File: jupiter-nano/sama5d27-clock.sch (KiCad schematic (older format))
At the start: 1 part

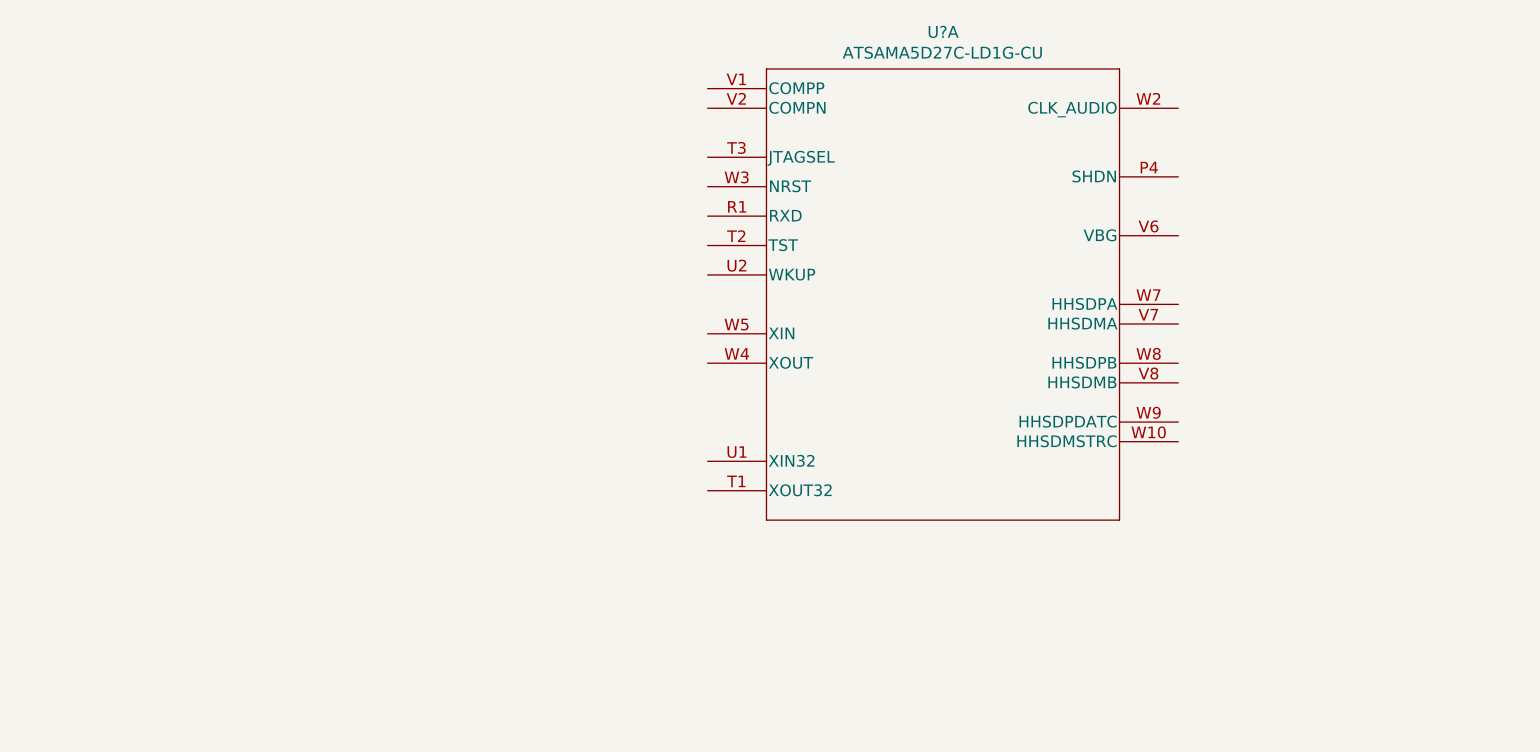
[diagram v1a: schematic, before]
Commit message: WIP some work on clocking
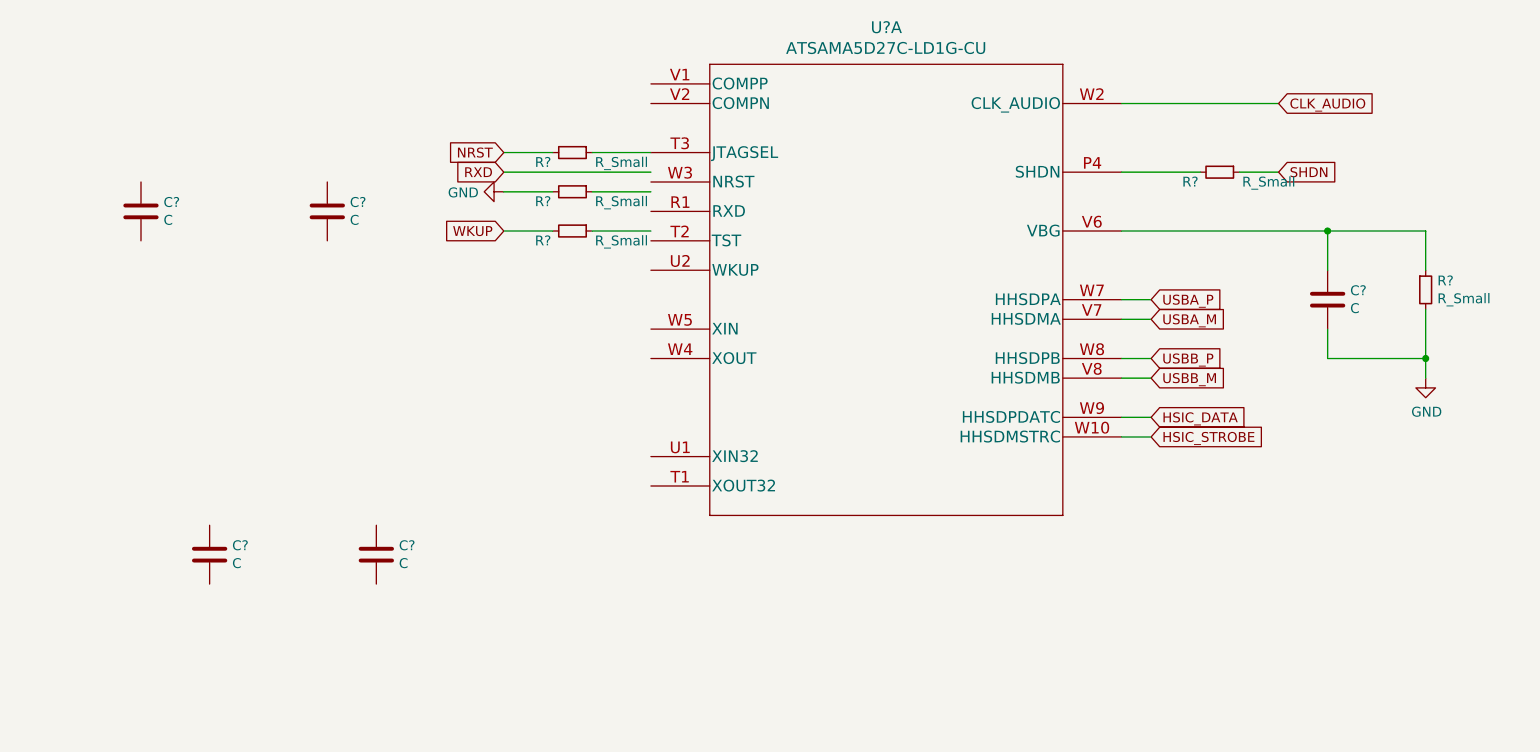
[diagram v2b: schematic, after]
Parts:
- added C? (x5): C, symbol Device:C
- added R? (x5): R_Small, symbol Device:R_Small
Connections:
- net labels added: CLK_AUDIO, GND, HSIC_DATA, HSIC_STROBE, NRST, RXD, SHDN, USBA_M, USBA_P, USBB_M, USBB_P, WKUP
- wire segments 0 -> 24
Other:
- moved on the sheet: U?A
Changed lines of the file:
@@
 L ATSAMA5D27C-LD1G:ATSAMA5D27C-LD1G-CU U?
 U 1 1 5F5D995F
-P 4739 2474
-F 0 "U?" H 5939 2961 60  0000 C CNN
-F 1 "ATSAMA5D27C-LD1G-CU" H 5939 2855 60  0000 C CNN
-F 2 "TFBGA361_16X16_MCH" H 5939 2814 60  0001 C CNN
-F 3 "" H 4739 2474 60  0000 C CNN
-	1    4739 2474
-	1    0    0    -1
-$EndComp
+P 4450 2450
+F 0 "U?" H 5650 2937 60  0000 C CNN
+F 1 "ATSAMA5D27C-LD1G-CU" H 5650 2831 60  0000 C CNN
+F 2 "TFBGA361_16X16_MCH" H 5650 2790 60  0001 C CNN
+F 3 "" H 4450 2450 60  0000 C CNN
+	1    4450 2450
+	1    0    0    -1
+$EndComp
+$Comp
+L Device:C C?
+U 1 1 5FB8C3A7
+P 1850 2900
+F 0 "C?" H 1965 2946 50  0000 L CNN
+F 1 "C" H 1965 2855 50  0000 L CNN
+F 2 "" H 1888 2750 50  0001 C CNN
+F 3 "~" H 1850 2900 50  0001 C CNN
+	1    1850 2900
+	1    0    0    -1
+$EndComp
+$Comp
+L Device:C C?
+U 1 1 5FB8D41E
+P 2800 2900
+F 0 "C?" H 2915 2946 50  0000 L CNN
+F 1 "C" H 2915 2855 50  0000 L CNN
+F 2 "" H 2838 2750 50  0001 C CNN
+F 3 "~" H 2800 2900 50  0001 C CNN
+	1    2800 2900
+	1    0    0    -1
+$EndComp
+$Comp
+L Device:C C?
+U 1 1 5FB8DCD9
+P 2200 4650
+F 0 "C?" H 2315 4696 50  0000 L CNN
+F 1 "C" H 2315 4605 50  0000 L CNN
+F 2 "" H 2238 4500 50  0001 C CNN
+F 3 "~" H 2200 4650 50  0001 C CNN
+	1    2200 4650
+	1    0    0    -1
+$EndComp
+$Comp
+L Device:C C?
+U 1 1 5FB8E15B
+P 3050 4650
+F 0 "C?" H 3165 4696 50  0000 L CNN
+F 1 "C" H 3165 4605 50  0000 L CNN
+F 2 "" H 3088 4500 50  0001 C CNN
+F 3 "~" H 3050 4650 50  0001 C CNN
+	1    3050 4650
+	1    0    0    -1
+$EndComp
+$Comp
+L Device:C C?
+U 1 1 5FB8E9C8
+P 7900 3350
+F 0 "C?" H 8015 3396 50  0000 L CNN
+F 1 "C" H 8015 3305 50  0000 L CNN
+F 2 "" H 7938 3200 50  0001 C CNN
+F 3 "~" H 7900 3350 50  0001 C CNN
+	1    7900 3350
+	1    0    0    -1
+$EndComp
+$Comp
+L Device:R_Small R?
+U 1 1 5FB8F66D
+P 8400 3300
+F 0 "R?" H 8459 3346 50  0000 L CNN
+F 1 "R_Small" H 8459 3255 50  0000 L CNN
+F 2 "" H 8400 3300 50  0001 C CNN
+F 3 "~" H 8400 3300 50  0001 C CNN
+	1    8400 3300
+	1    0    0    -1
+$EndComp
+$Comp
+L Device:R_Small R?
+U 1 1 5FB9019B
+P 4050 2600
+F 0 "R?" V 4100 2450 50  0000 C CNN
+F 1 "R_Small" V 4100 2850 50  0000 C CNN
+F 2 "" H 4050 2600 50  0001 C CNN
+F 3 "~" H 4050 2600 50  0001 C CNN
+	1    4050 2600
+	0    1    1    0
+$EndComp
+$Comp
+L Device:R_Small R?
+U 1 1 5FB90BC4
+P 4050 3000
+F 0 "R?" V 4100 2850 50  0000 C CNN
+F 1 "R_Small" V 4100 3250 50  0000 C CNN
+F 2 "" H 4050 3000 50  0001 C CNN
+F 3 "~" H 4050 3000 50  0001 C CNN
+	1    4050 3000
+	0    1    1    0
+$EndComp
+$Comp
+L Device:R_Small R?
+U 1 1 5FB913F4
+P 7350 2700
+F 0 "R?" V 7400 2550 50  0000 C CNN
+F 1 "R_Small" V 7400 2950 50  0000 C CNN
+F 2 "" H 7350 2700 50  0001 C CNN
+F 3 "~" H 7350 2700 50  0001 C CNN
+	1    7350 2700
+	0    1    1    0
+$EndComp
+$Comp
+L Device:R_Small R?
+U 1 1 5FB91AFA
+P 4050 2800
+F 0 "R?" V 4100 2650 50  0000 C CNN
+F 1 "R_Small" V 4100 3050 50  0000 C CNN
+F 2 "" H 4050 2800 50  0001 C CNN
+F 3 "~" H 4050 2800 50  0001 C CNN
+	1    4050 2800
+	0    1    1    0
+$EndComp
+Wire Wire Line
+	4450 2600 4150 2600
+Wire Wire Line
+	3950 2600 3700 2600
+Text GLabel 3700 2600 0    50   Input ~ 0
+NRST
+Text GLabel 3700 3000 0    50   Input ~ 0
+WKUP
+Wire Wire Line
+	4150 3000 4450 3000
+Wire Wire Line
+	3950 3000 3700 3000
+Wire Wire Line
+	6850 2700 7250 2700
+Wire Wire Line
+	7450 2700 7650 2700
+Text GLabel 7650 2700 2    50   Input ~ 0
+SHDN
+Wire Wire Line
+	4150 2800 4450 2800
+Wire Wire Line
+	3700 2800 3950 2800
+$Comp
+L power:GND #PWR?
+U 1 1 5FBB7C84
+P 3700 2800
+F 0 "#PWR?" H 3700 2550 50  0001 C CNN
+F 1 "GND" V 3705 2672 50  0000 R CNN
+F 2 "" H 3700 2800 50  0001 C CNN
+F 3 "" H 3700 2800 50  0001 C CNN
+	1    3700 2800
+	0    1    1    0
+$EndComp
+Wire Wire Line
+	4450 2700 3700 2700
+Text GLabel 3700 2700 0    50   Input ~ 0
+RXD
+Wire Wire Line
+	6850 2350 7650 2350
+Text GLabel 7650 2350 2    50   Input ~ 0
+CLK_AUDIO
+Wire Wire Line
+	6850 3000 7900 3000
+Wire Wire Line
+	7900 3000 7900 3200
+Wire Wire Line
+	7900 3000 8400 3000
+Wire Wire Line
+	8400 3000 8400 3200
+Connection ~ 7900 3000
+Wire Wire Line
+	8400 3400 8400 3650
+Wire Wire Line
+	8400 3650 7900 3650
+Wire Wire Line
+	7900 3650 7900 3500
+Wire Wire Line
+	8400 3650 8400 3750
+Connection ~ 8400 3650
+$Comp
+L power:GND #PWR?
+U 1 1 5FBD26A3
+P 8400 3750
+F 0 "#PWR?" H 8400 3500 50  0001 C CNN
+F 1 "GND" H 8405 3577 50  0000 C CNN
+F 2 "" H 8400 3750 50  0001 C CNN
+F 3 "" H 8400 3750 50  0001 C CNN
+	1    8400 3750
+	1    0    0    -1
+$EndComp
+Wire Wire Line
+	6850 3950 7000 3950
+Wire Wire Line
+	6850 4050 7000 4050
+Wire Wire Line
+	6850 3750 7000 3750
+Wire Wire Line
+	6850 3650 7000 3650
+Wire Wire Line
+	6850 3450 7000 3450
+Wire Wire Line
+	6850 3350 7000 3350
+Text GLabel 7000 3350 2    50   Input ~ 0
+USBA_P
+Text GLabel 7000 3450 2    50   Input ~ 0
+USBA_M
+Text GLabel 7000 3650 2    50   Input ~ 0
+USBB_P
+Text GLabel 7000 3750 2    50   Input ~ 0
+USBB_M
+Text GLabel 7000 3950 2    50   Input ~ 0
+HSIC_DATA
+Text GLabel 7000 4050 2    50   Input ~ 0
+HSIC_STROBE
 $EndSCHEMATC

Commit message: WIP clocking done
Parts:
- removed C?: C, symbol Device:C
- added C97: 8pF 50V, symbol Device:C
- added Y1: NX2012SA-32.768KHZ-EXS00A-MU00389, symbol Device:Crystal
- added Y2: NX3225SA-12MHZ-STD-CSR-3, symbol Device:Crystal_GND24
- C96: renamed from C?; value C -> 8pF 50V
- C98, C99: renamed from C?; value C -> 27pF 50V
- gave numbers to parts that had none: 1
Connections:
- wire segments 24 -> 47
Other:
- moved on the sheet: C96, C98, C99, R?

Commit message: WIP, PIO done
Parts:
- C98, C99: value 27pF 50V -> 16pF 50V
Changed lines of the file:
@@
 P 1300 3900
 F 0 "C98" H 1415 3946 50  0000 L CNN
-F 1 "27pF 50V" H 1415 3855 50  0000 L CNN
+F 1 "16pF 50V" H 1415 3855 50  0000 L CNN
 F 2 "" H 1338 3750 50  0001 C CNN
 F 3 "~" H 1300 3900 50  0001 C CNN
@@
 P 2250 3900
 F 0 "C99" H 2365 3946 50  0000 L CNN
-F 1 "27pF 50V" H 2365 3855 50  0000 L CNN
+F 1 "16pF 50V" H 2365 3855 50  0000 L CNN
 F 2 "" H 2288 3750 50  0001 C CNN
 F 3 "~" H 2250 3900 50  0001 C CNN

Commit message: WIP, connectors almost done
- still to do:
  - JTAG signals on PIO pins
  - USB-UART bridge
  - extra PIO on the header pins
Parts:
- added NT1: Net-Tie_2, symbol Device:Net-Tie_2
- C100: renamed from C?; value C -> 10pF 25V
- R27: renamed from R?; value R_Small -> 100R 1%
- R28: renamed from R?; value R_Small -> 5.6K
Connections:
- net GND: now also NT1.2; no longer C100.2, R28.2
- new net: C100.2, NT1.1, R28.2
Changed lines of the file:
@@
 $EndComp
 $Comp
-L Device:C C?
+L Device:C C100
 U 1 1 5FB8E9C8
 P 7900 3350
-F 0 "C?" H 8015 3396 50  0000 L CNN
-F 1 "C" H 8015 3305 50  0000 L CNN
+F 0 "C100" H 7950 3450 50  0000 L CNN
+F 1 "10pF 25V" H 7950 3250 50  0000 L CNN
 F 2 "" H 7938 3200 50  0001 C CNN
 F 3 "~" H 7900 3350 50  0001 C CNN
 	1    7900 3350
-	1    0    0    -1
-$EndComp
-$Comp
-L Device:R_Small R?
-U 1 1 5FB8F66D
-P 8400 3300
-F 0 "R?" H 8459 3346 50  0000 L CNN
-F 1 "R_Small" H 8459 3255 50  0000 L CNN
-F 2 "" H 8400 3300 50  0001 C CNN
-F 3 "~" H 8400 3300 50  0001 C CNN
-	1    8400 3300
 	1    0    0    -1
 $EndComp
@@
 $EndComp
 $Comp
-L Device:R_Small R?
+L Device:R_Small R27
 U 1 1 5FB913F4
 P 7350 2700
-F 0 "R?" V 7400 2550 50  0000 C CNN
-F 1 "R_Small" V 7400 2950 50  0000 C CNN
+F 0 "R27" V 7250 2700 50  0000 C CNN
+F 1 "100R 1%" V 7450 2750 50  0000 C CNN
 F 2 "" H 7350 2700 50  0001 C CNN
 F 3 "~" H 7350 2700 50  0001 C CNN
@@
 L power:GND #PWR?
 U 1 1 5FBD26A3
-P 8400 3750
-F 0 "#PWR?" H 8400 3500 50  0001 C CNN
-F 1 "GND" H 8405 3577 50  0000 C CNN
-F 2 "" H 8400 3750 50  0001 C CNN
-F 3 "" H 8400 3750 50  0001 C CNN
-	1    8400 3750
+P 8400 4050
+F 0 "#PWR?" H 8400 3800 50  0001 C CNN
+F 1 "GND" H 8405 3877 50  0000 C CNN
+F 2 "" H 8400 4050 50  0001 C CNN
+F 3 "" H 8400 4050 50  0001 C CNN
+	1    8400 4050
 	1    0    0    -1
 $EndComp
@@
 	1    0    0    -1
 $EndComp
+$Comp
+L Device:Net-Tie_2 NT1
+U 1 1 601349A6
+P 8400 3850
+F 0 "NT1" V 8354 3894 50  0000 L CNN
+F 1 "Net-Tie_2" V 8445 3894 50  0000 L CNN
+F 2 "" H 8400 3850 50  0001 C CNN
+F 3 "~" H 8400 3850 50  0001 C CNN
+	1    8400 3850
+	0    1    1    0
+$EndComp
+Wire Wire Line
+	8400 3950 8400 4050
+$Comp
+L Device:R_Small R28
+U 1 1 5FB8F66D
+P 8400 3300
+F 0 "R28" H 8459 3346 50  0000 L CNN
+F 1 "5.6K" H 8459 3255 50  0000 L CNN
+F 2 "" H 8400 3300 50  0001 C CNN
+F 3 "~" H 8400 3300 50  0001 C CNN
+	1    8400 3300
+	1    0    0    -1
+$EndComp

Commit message: reset logic R names, values; longer connnectors
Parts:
- R24, R25: renamed from R?; value R_Small -> 100R 1%
- R26: renamed from R?; value R_Small -> 10K
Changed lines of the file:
@@
 $EndComp
 $Comp
-L Device:R_Small R?
+L Device:R_Small R24
 U 1 1 5FB9019B
 P 4150 2750
-F 0 "R?" V 4200 2600 50  0000 C CNN
-F 1 "R_Small" V 4200 3000 50  0000 C CNN
+F 0 "R24" V 4200 2600 50  0000 C CNN
+F 1 "100R 1%" V 4200 3000 50  0000 C CNN
 F 2 "" H 4150 2750 50  0001 C CNN
 F 3 "~" H 4150 2750 50  0001 C CNN
@@
 $EndComp
 $Comp
-L Device:R_Small R?
+L Device:R_Small R26
 U 1 1 5FB90BC4
 P 4200 3200
-F 0 "R?" V 4250 3050 50  0000 C CNN
-F 1 "R_Small" V 4250 3450 50  0000 C CNN
+F 0 "R26" V 4250 3050 50  0000 C CNN
+F 1 "10K" V 4250 3450 50  0000 C CNN
 F 2 "" H 4200 3200 50  0001 C CNN
 F 3 "~" H 4200 3200 50  0001 C CNN
@@
 $EndComp
 $Comp
-L Device:R_Small R?
+L Device:R_Small R25
 U 1 1 5FB91AFA
 P 4150 3050
-F 0 "R?" V 4200 2900 50  0000 C CNN
-F 1 "R_Small" V 4200 3300 50  0000 C CNN
+F 0 "R25" V 4200 2900 50  0000 C CNN
+F 1 "100R 1%" V 4200 3300 50  0000 C CNN
 F 2 "" H 4150 3050 50  0001 C CNN
 F 3 "~" H 4150 3050 50  0001 C CNN
